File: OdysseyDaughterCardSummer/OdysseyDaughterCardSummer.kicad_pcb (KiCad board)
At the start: 2 copper layers, 46.5 x 46.6 mm, 26 parts, among them J1 Conn_01x03, J2 Conn_01x02, J3 Conn_Coaxial, U1 TLV3542, X1 OdysseyDaughterCard

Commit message: OdysseyDaughterCardSummer: Open and close in KiCad 6, fix symbol library path
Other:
- net class Default removed

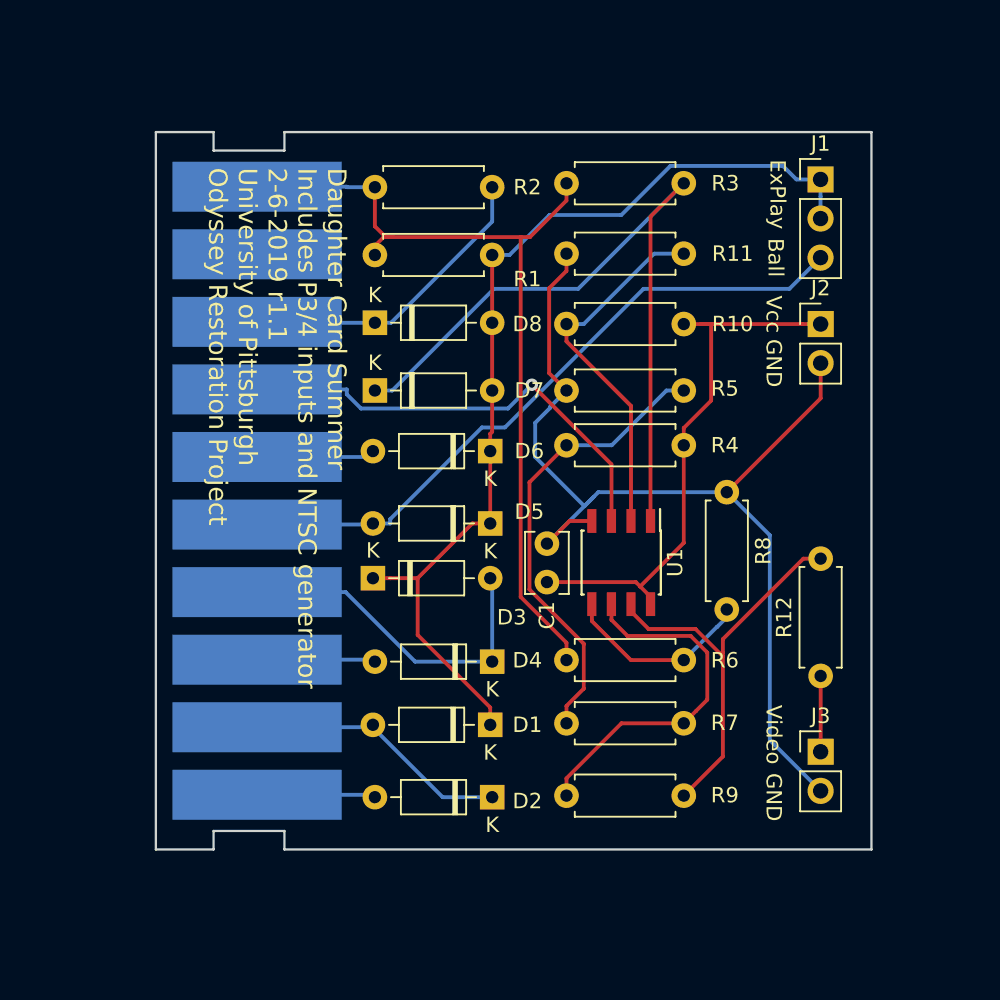
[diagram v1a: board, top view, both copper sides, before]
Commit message: OdysseyDaughterCardSummer add logo, generate pdf, images, 3d models
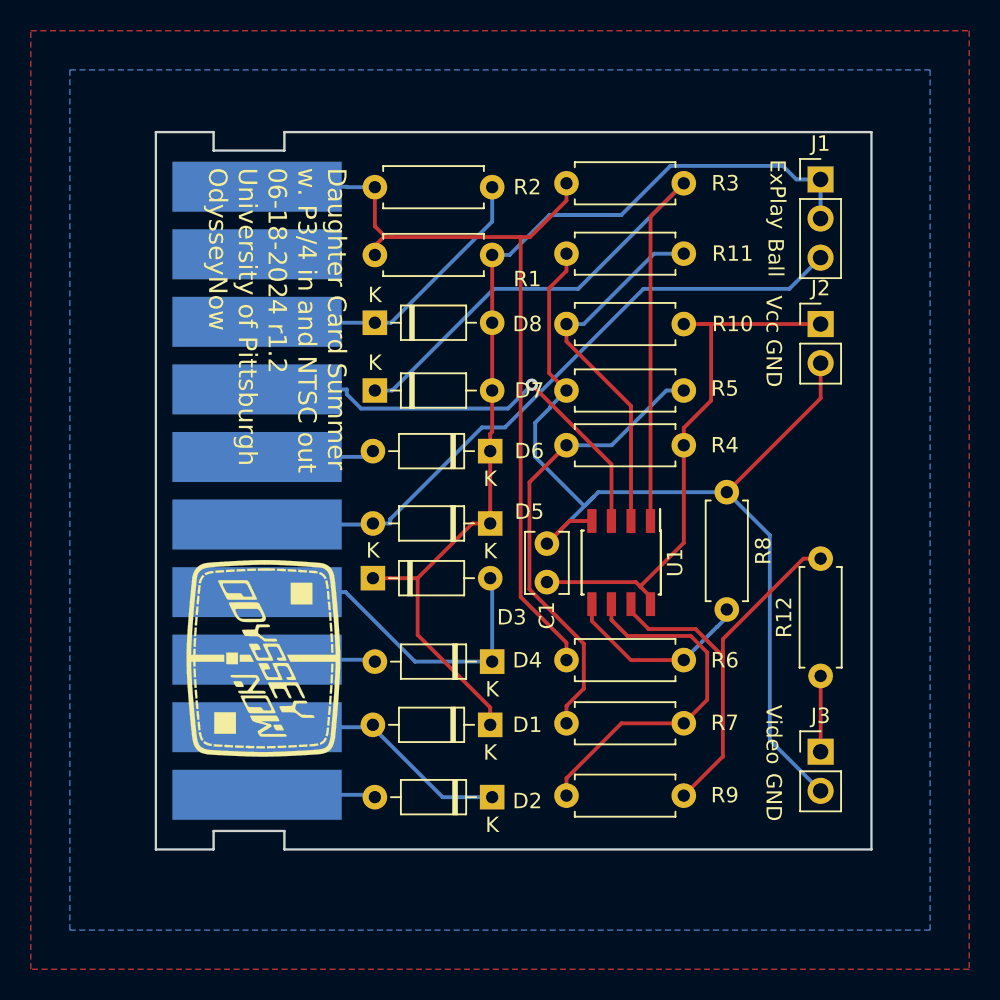
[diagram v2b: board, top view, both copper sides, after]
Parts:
- added X2: OdysseyNow_Logo, Odyssey_Daughter_Card:OdysseyNowLogo, F.Cu at (130.2, 111.6)
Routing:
- added copper zone on B.Cu, net GND
- added copper zone on F.Cu, net VCC
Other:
- board text added: "Daughter Card Summer w. P3/4 in and NTSC out 06-18-2024 r1.2 University of Pittsburgh OdysseyNow"
- board text removed: "Daughter Card Summer Includes P3/4 inputs and NTSC generator 2-6-2019 r1.1 University of Pittsburgh Odyssey Restoration Project"
